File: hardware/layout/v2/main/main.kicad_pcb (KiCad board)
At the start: 4 copper layers, 31.5 x 76.5 mm, 48 parts, among them J1 KNX bus terminal pins, J2 AUX, J3 DALI, J4 Controller cable, J5 Interface DALI, J6 Interface logic, Q1 MJD45H11, Q2 BC857, U1 NCN5130MNTWG, U2 SCT2400TVBR, U3 REM3-2415S/A 24V->15V 3W iso, Y1 16MHz

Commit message: V3 hardware complete: four boards routed and released with 1-DIN enclosure; CI matrix updated; REM3/CTRL supply-off circuit added
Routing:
- net GND: track 169.3 -> 151.8 mm, vias 2 -> 1
- net DALI_TX: track 28.9 -> 18.6 mm
- net KNX_TXD: track 27.6 -> 36.4 mm
- net +3V3_TRX: track 47.5 -> 39.6 mm
- net DALI_RX: track 23.6 -> 17.2 mm
- net VFILT: track 59.9 -> 65.6 mm, vias 1 -> 2
- net VDD1M: track 16.5 -> 12.0 mm
- net N$3: track 12.2 -> 16.6 mm
- net +3V3: track 24.8 -> 20.6 mm
- net N$1: track 13.3 -> 10.0 mm
- net KNX_P: track 14.3 -> 11.9 mm, vias 1 -> 0
- net VSW1: track 5.61 -> 7.90 mm, vias 1 -> 2
- net GNDD: track 49.9 -> 47.8 mm
- net NCN_SAVEB: track 43.7 -> 42.0 mm, vias 2 -> 3
- net DALI_SUPPLY_SW: track 28.3 -> 29.9 mm, vias 1 -> 2
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
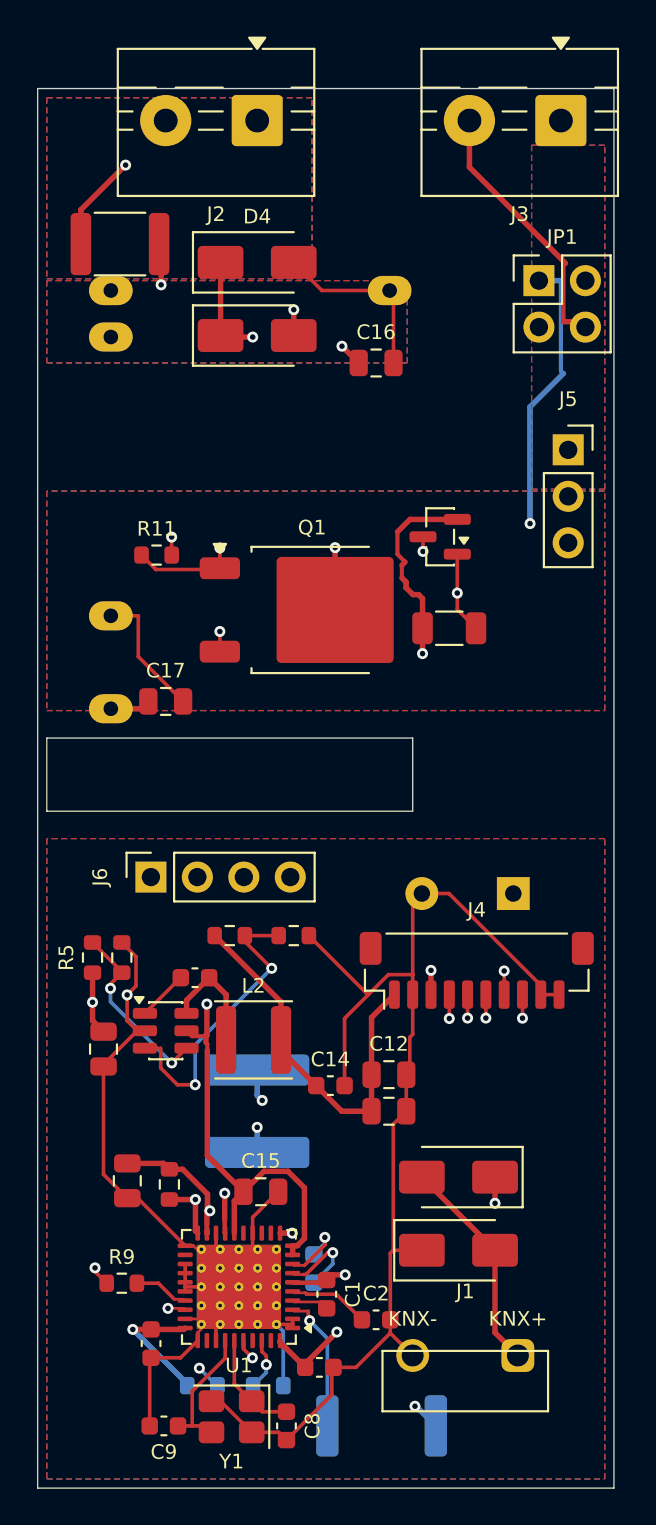
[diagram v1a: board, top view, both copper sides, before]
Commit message: V3 consolidated to two boards (main + ui); updated firmware pin map, button ADC, and OLED connector; removed separate knx/dali boards from CI matrix
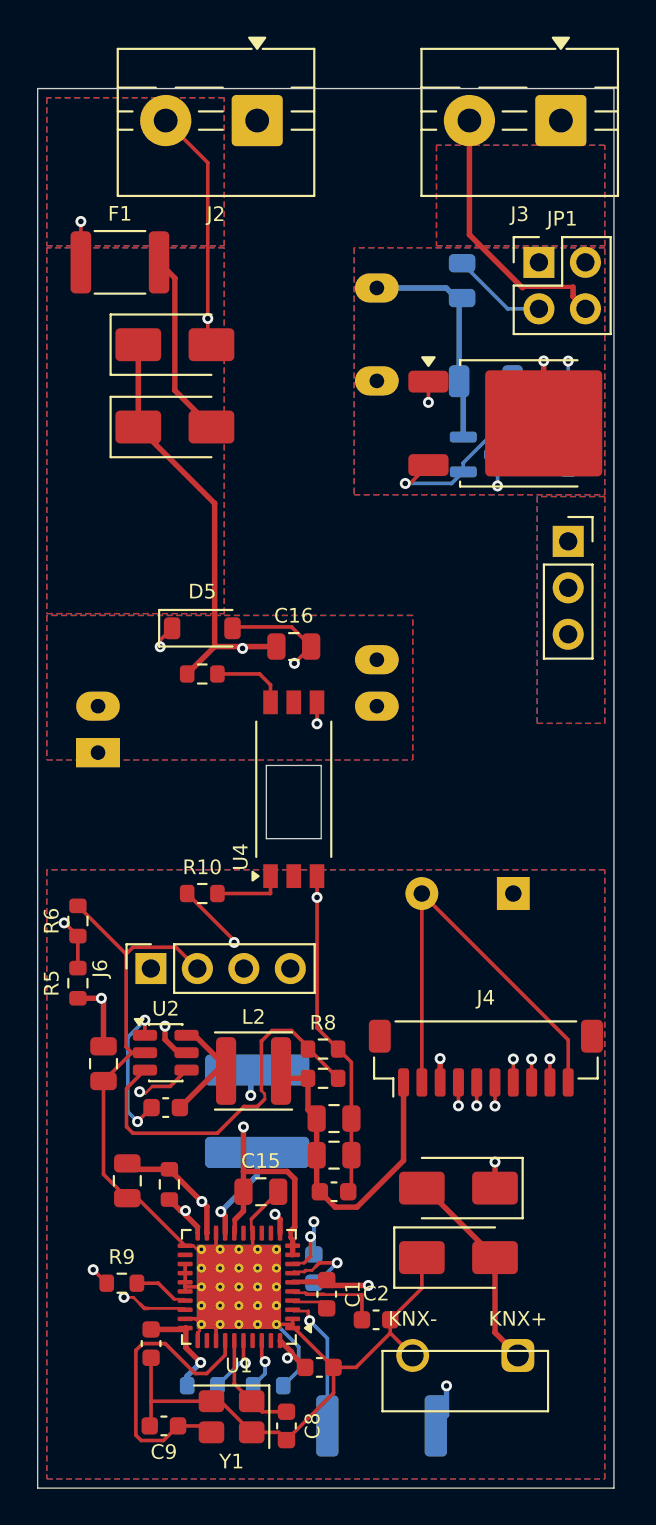
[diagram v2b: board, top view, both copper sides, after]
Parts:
- added D5: 5V6, Diode_SMD:D_SOD-123, F.Cu at (9.00, -47.0)
- added R12: 3R3, Resistor_SMD:R_1206_3216Metric, B.Cu at (24.5, -60.5)
- added R13: 4k7, Resistor_SMD:R_0603_1608Metric, B.Cu at (29.0, -56.5)
- added U4: TLP383, Package_SO:SO-6L_10x3.84mm_P1.27mm, F.Cu at (14.0, -38.2)
- C17, Q2: moved to B.Cu
- R10: value 3R3 -> 330R; footprint Resistor_SMD:R_1206_3216Metric -> Resistor_SMD:R_0603_1608Metric
- R11: value 4k7 -> 10k
- U3: value REM3-2415S/A 24V->15V 3W iso -> REM3-2415S/A/CTRL 24V->15V 3W iso; footprint gateway_fp:Converter_DCDC_RECOM_REM3_DIP24 -> gateway_fp:Converter_DCDC_RECOM_REM3_DIP24_CTRL
- moved U3 32.0 mm to (3.30, -40.2), turned to 0 degrees
- moved C17 28.1 mm to (23.2, -66.0), turned to 90 degrees
- moved R10 19.8 mm to (9.00, -32.5)
- moved C16 16.1 mm to (14.0, -46.0)
- moved Q1 15.3 mm to (26.4, -58.2)
- moved R7 9.32 mm to (15.6, -22.4)
- moved C10 7.28 mm to (7.00, -20.8)
- moved R11 6.96 mm to (9.00, -44.5)
- moved D3 6.73 mm to (7.50, -58.0)
- moved R8 6.40 mm to (15.6, -24.0)
- moved D4 6.36 mm to (7.50, -62.5)
- moved C14 5.80 mm to (16.2, -16.2)
- moved Q2 5.01 mm to (24.2, -56.5), turned to 0 degrees
- moved J5 5.00 mm to (29.0, -51.8)
- moved J6 5.00 mm to (6.19, -28.4)
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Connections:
- J4 pad 9: GND -> DALI_SUPPLY_OFF
- Q1 pad 1: N$7 -> N$10
- Q1 pad 3: N$6 -> N$9
- Q2 pad 1: N$6 -> N$9
- Q2 pad 3: N$7 -> N$10
- R10 pad 1: DALI_ISO15V -> DALI_SUPPLY_OFF
- R11 pad 1: N$7 -> AUX_P
- R11 pad 2: GNDD -> N$7
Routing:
- net N$8: track 0.00 -> 25.6 mm, vias 0 -> 2
- net DALI_SUPPLY_OFF: track 0.00 -> 25.1 mm, vias 0 -> 2
- net DALI_SUPPLY_SW: track 29.9 -> 10.1 mm, vias 2 -> 1
- net DALI_ISO15V: track 31.6 -> 12.6 mm, vias 1 -> 0
- net GNDA: track 32.0 -> 50.2 mm, vias 0 -> 2
- net N$6: track 19.4 -> 3.86 mm, vias 2 -> 0
- net NCN_SAVEB: track 42.0 -> 26.8 mm, vias 3 -> 2
- net N$7: track 18.1 -> 4.10 mm, vias 2 -> 0
- net N$10: track 0.00 -> 13.2 mm, vias 0 -> 2
- net AUX_P: track 24.0 -> 35.5 mm, vias 2 -> 1
- net N$9: track 0.00 -> 11.2 mm, vias 0 -> 1
- net GNDD: track 47.8 -> 38.3 mm
- net XTAL2: track 7.38 -> 16.3 mm
- net VFILT: track 65.6 -> 57.4 mm, vias 2 -> 3
- net GND: track 151.8 -> 158.7 mm
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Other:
- outline, holes or cut-outs redrawn
